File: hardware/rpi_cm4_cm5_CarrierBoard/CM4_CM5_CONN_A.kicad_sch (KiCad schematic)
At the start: 53 parts, among them J19 RPI_CMx_A, J7 2998TR, Q12 2N7002, U19 SN74LVC1G125DBVR, U21 MCP7940NT-I/MS, Y2 32.768kHz

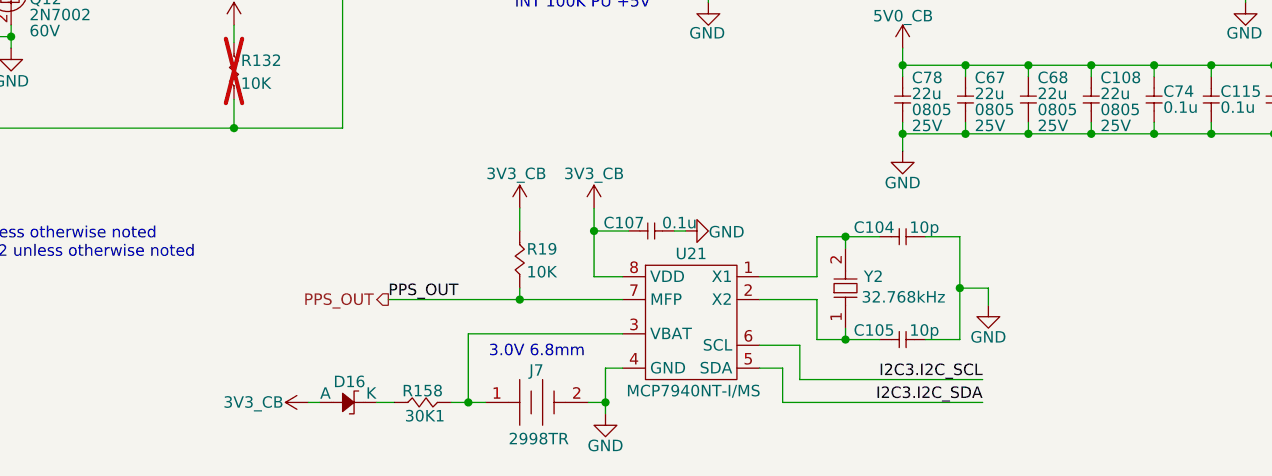
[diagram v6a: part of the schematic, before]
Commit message: Add preliminary output files (PCB PDF, Gerbers, IPC-D-356, IPC-2581, Pick_N_Place, etc) Update BOM, SCH PDF Commit PCB design and set to "Review" state
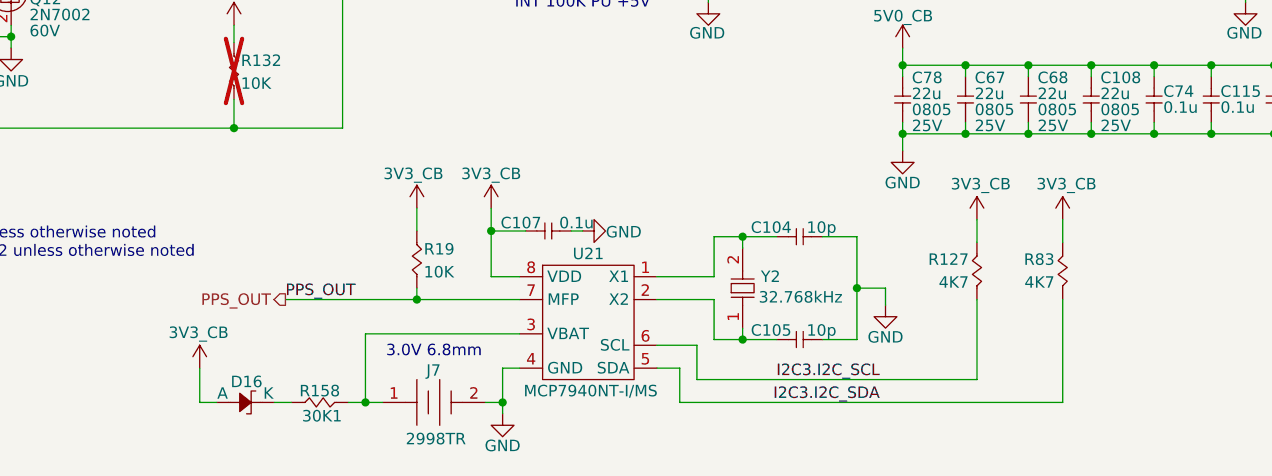
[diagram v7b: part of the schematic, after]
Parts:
- added R127, R83: 4K7, footprint:RES_0402, symbol KicadCompDb:Resistors/RES_SMT_00010
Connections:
- net 3V3_CB: now also R127.2, R83.2
- net I2C3.I2C_SCL: now also R127.1
- net I2C3.I2C_SDA: now also R83.1
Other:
- moved on the sheet: C104, C105, C107, D16, J7, R158, R19, U21, Y2

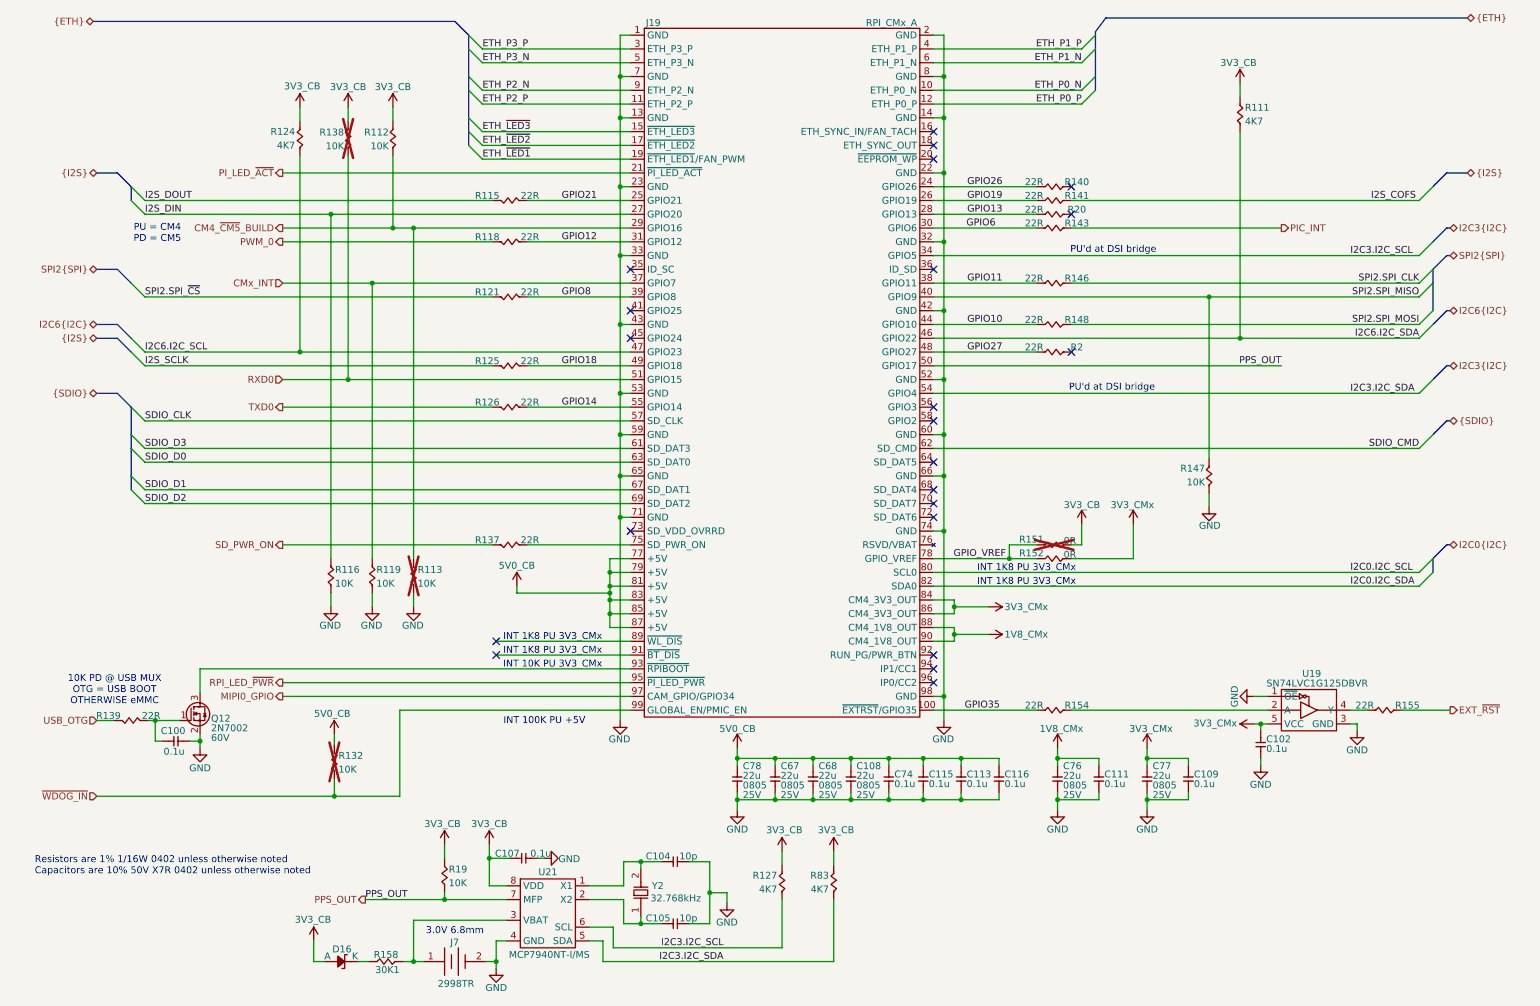
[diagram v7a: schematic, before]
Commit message: Add test points on relevant signals Re-generate SCH_PDF Re-generate BOM Re-generate all gerbers and relevant PCB output files (still in review phase)
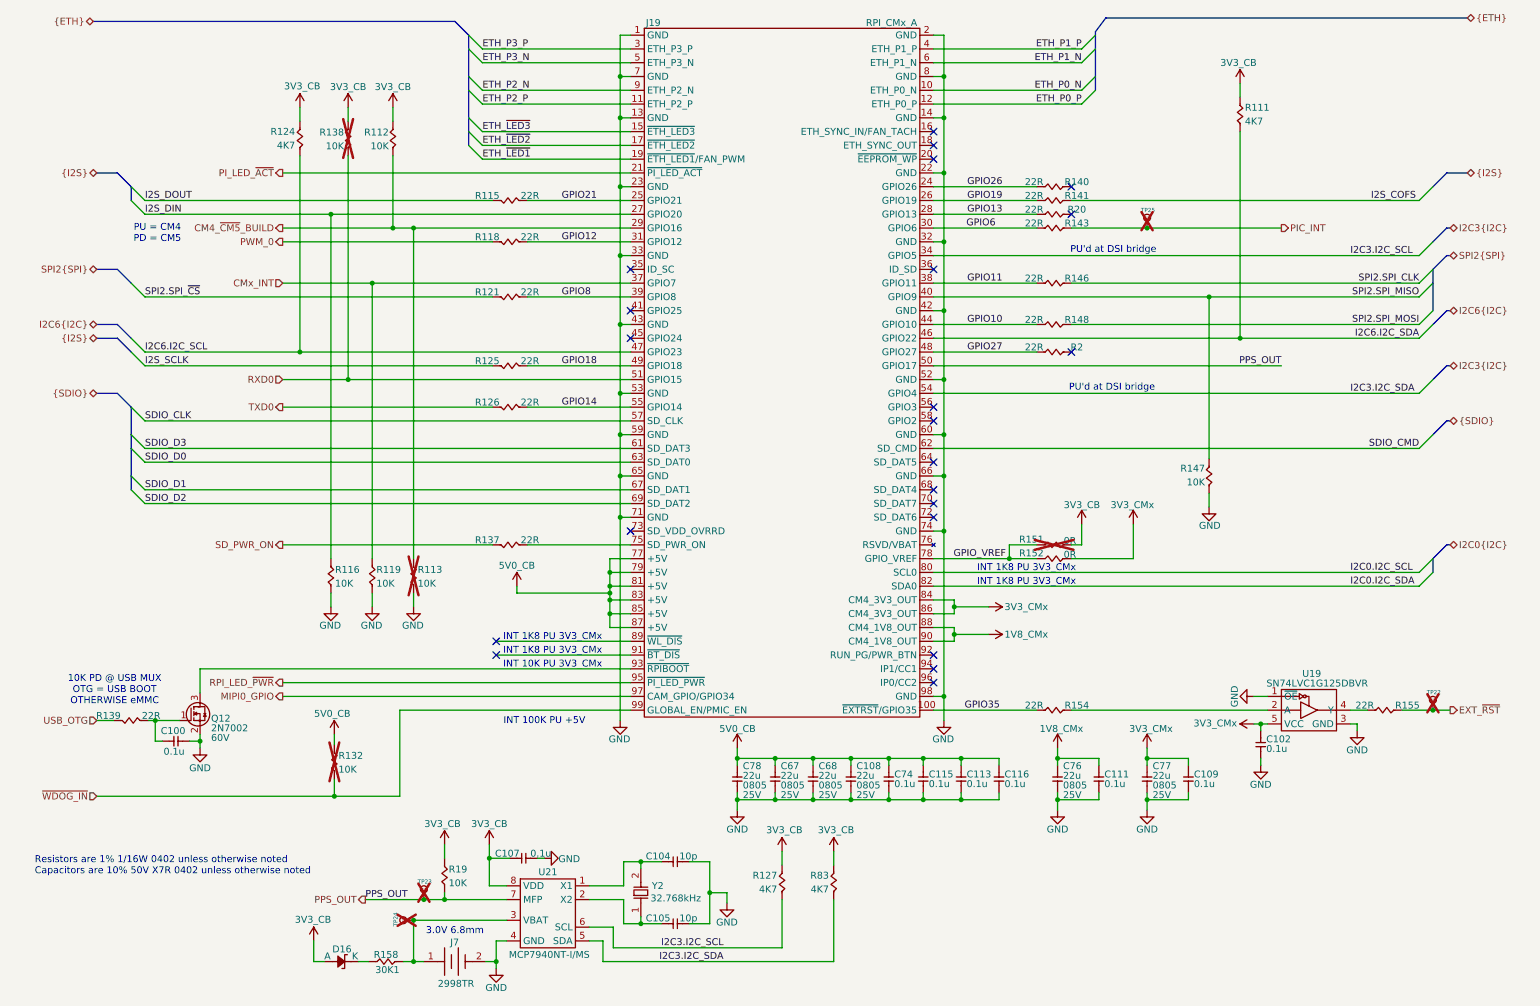
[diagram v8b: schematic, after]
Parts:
- added TP22, TP23, TP24, TP25: 28 mils, footprint:SMT_TP_28_MILS, symbol KicadCompDb:Test Point/TP_00001
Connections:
- net EXT_~{RST}: now also TP22.1
- net PIC_INT: now also TP25.1
- net PPS_OUT: now also TP23.1
- net at J7.1, R158.1, U21.3 (VBAT): now also TP24.1
